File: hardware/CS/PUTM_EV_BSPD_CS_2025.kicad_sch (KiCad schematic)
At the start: 35 parts, among them J2 LEM, J3 Conn_01x04, U1 MC78M12CDTG, U2 LM1117IMP-5.0, U3 TLV9354QPWRQ1

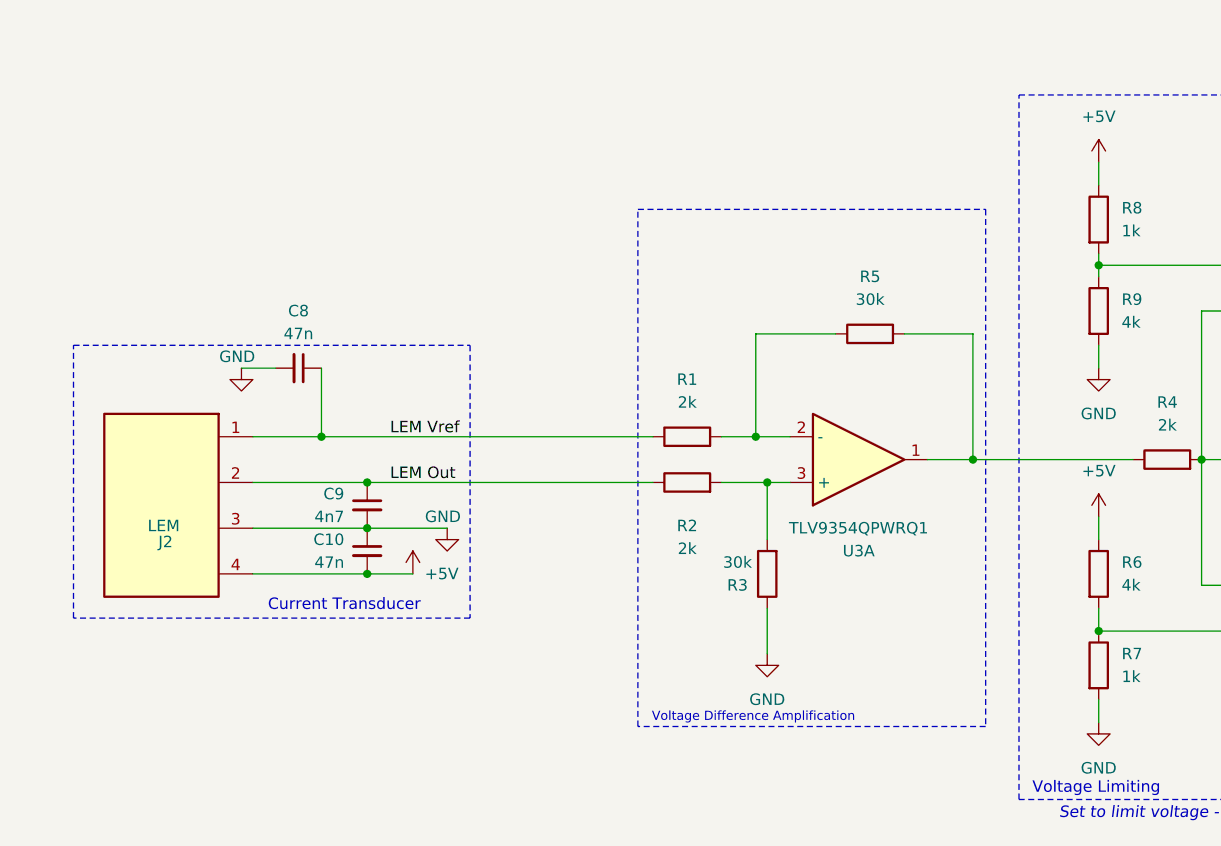
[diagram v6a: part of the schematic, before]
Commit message: CS gain fix, Added comments
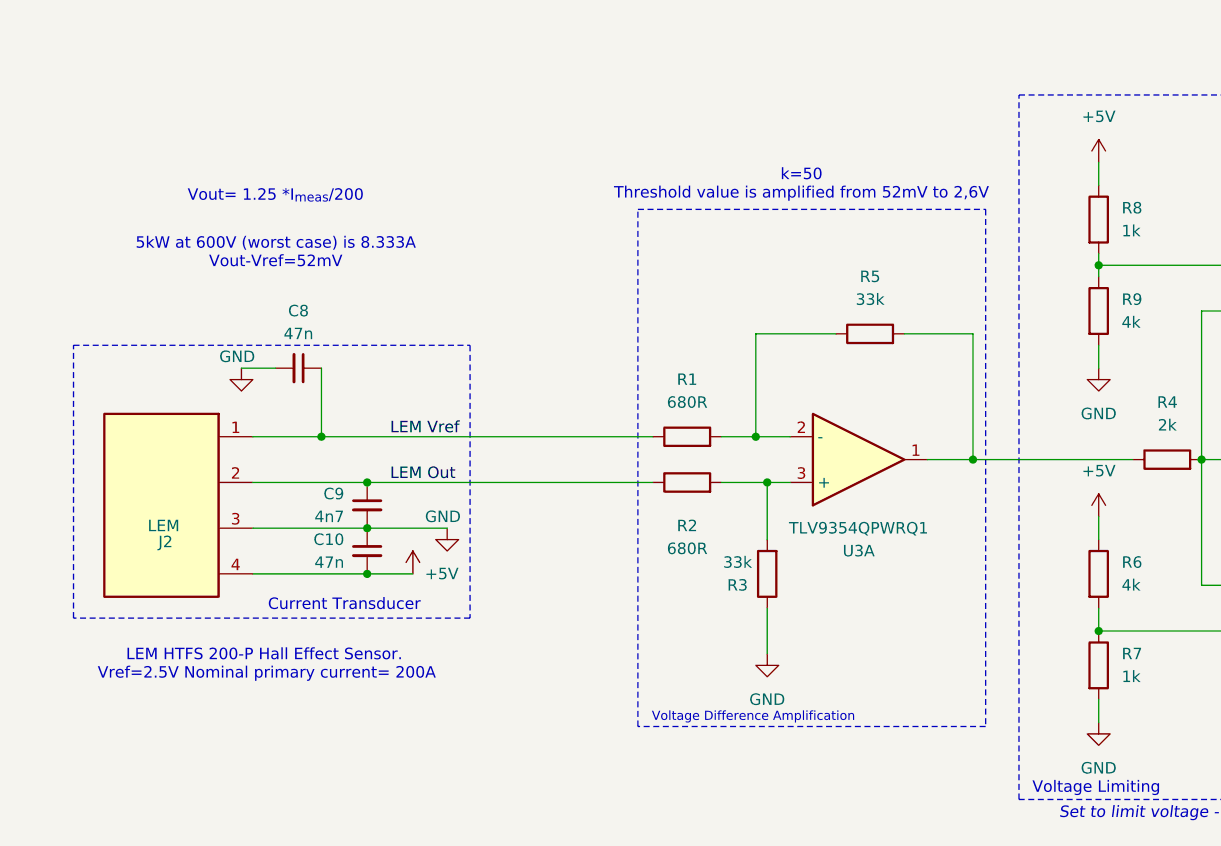
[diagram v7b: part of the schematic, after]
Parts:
- R1, R2: value 2k -> 680R
- R3, R5: value 30k -> 33k
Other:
- note added: "5kW at 600V (worst case) is 8.333A Vout-Vref=52mV"
- note added: "LEM HTFS 200-P Hall Effect Sensor. Vref=2.5V Nominal primary current= 200A"
- note added: "Vout= 1.25 *I_{meas}/200"
- note added: "k=50 Threshold value is amplified from 52mV to 2,6V"
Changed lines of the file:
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@@
 		(rev "${REVISION}")
 		(company "Author:")
-		(comment 1 "Reviewer:")
+		(comment 1 "Reviewer: Przemysław Zioła, Piotr Lesicki")
 	)
 	(rectangle
@@
 		)
 	)
+	(text "k=50\nThreshold value is amplified from 52mV to 2,6V"
+		(exclude_from_sim no)
+		(at 99.06 76.2 0)
+		(effects
+			(font
+				(size 1.27 1.27)
+			)
+		)
+	)
+	(text "5kW at 600V (worst case) is 8.333A\nVout-Vref=52mV"
+		(exclude_from_sim no)
+		(at 40.64 83.82 0)
+		(effects
+			(font
+				(size 1.27 1.27)
+			)
+		)
+	)
 	(text "BSPD Current Sensor Board"
 		(exclude_from_sim no)
@@
 		)
 	)
+	(text "LEM HTFS 200-P Hall Effect Sensor.\n Vref=2.5V Nominal primary current= 200A"
+		(exclude_from_sim no)
+		(at 39.37 129.54 0)
+		(effects
+			(font
+				(size 1.27 1.27)
+			)
+		)
+	)
 	(text "Power Section + IC Debounce"
 		(exclude_from_sim no)
@@
 		)
 	)
+	(text "Vout= 1.25 *I_{meas}/200"
+		(exclude_from_sim no)
+		(at 40.64 77.47 0)
+		(effects
+			(font
+				(size 1.27 1.27)
+			)
+		)
+	)
 	(text "Current Transducer"
 		(exclude_from_sim no)
@@
 			)
 		)
-		(property "Value" "30k"
+		(property "Value" "33k"
 			(at 91.948 118.11 0)
 			(effects
@@
 			)
 		)
+		(property "Mouser#" ""
+			(at 95.25 119.38 0)
+			(effects
+				(font
+					(size 1.27 1.27)
+				)
+				(hide yes)
+			)
+		)
+		(property "TME#" ""
+			(at 95.25 119.38 0)
+			(effects
+				(font
+					(size 1.27 1.27)
+				)
+				(hide yes)
+			)
+		)
 		(pin "1"
 		)
@@
 			)
 		)
-		(property "Value" "2k"
+		(property "Value" "680R"
 			(at 86.36 100.33 90)
 			(effects
@@
 			)
 		)
+		(property "Mouser#" ""
+			(at 86.36 104.14 0)
+			(effects
+				(font
+					(size 1.27 1.27)
+				)
+				(hide yes)
+			)
+		)
+		(property "TME#" ""
+			(at 86.36 104.14 0)
+			(effects
+				(font
+					(size 1.27 1.27)
+				)
+				(hide yes)
+			)
+		)
 		(pin "2"
 		)
@@
 			)
 		)
-		(property "Value" "2k"
+		(property "Value" "680R"
 			(at 86.36 116.586 90)
 			(effects
@@
 			)
 		)
+		(property "Mouser#" ""
+			(at 86.36 109.22 0)
+			(effects
+				(font
+					(size 1.27 1.27)
+				)
+				(hide yes)
+			)
+		)
+		(property "TME#" ""
+			(at 86.36 109.22 0)
+			(effects
+				(font
+					(size 1.27 1.27)
+				)
+				(hide yes)
+			)
+		)
 		(pin "1"
 		)
@@
 			)
 		)
-		(property "Value" "30k"
+		(property "Value" "33k"
 			(at 106.68 88.9 90)
 			(effects
@@
 			(at 106.68 92.71 0)
 			(effects
+				(font
+					(size 1.27 1.27)
+				)
+				(hide yes)
+			)
+		)
+		(property "Mouser#" ""
+			(at 106.68 92.71 0)
+			(effects
+				(font
+					(size 1.27 1.27)
+				)
+				(hide yes)
+			)
+		)
+		(property "TME#" ""
+			(at 106.68 92.71 0)
+			(effects
